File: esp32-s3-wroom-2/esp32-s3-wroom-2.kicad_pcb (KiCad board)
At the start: 4 copper layers, 11 parts, among them SW1 SW_Push, SW2 SW_Push, U1 ESP32-S3-WROOM-2

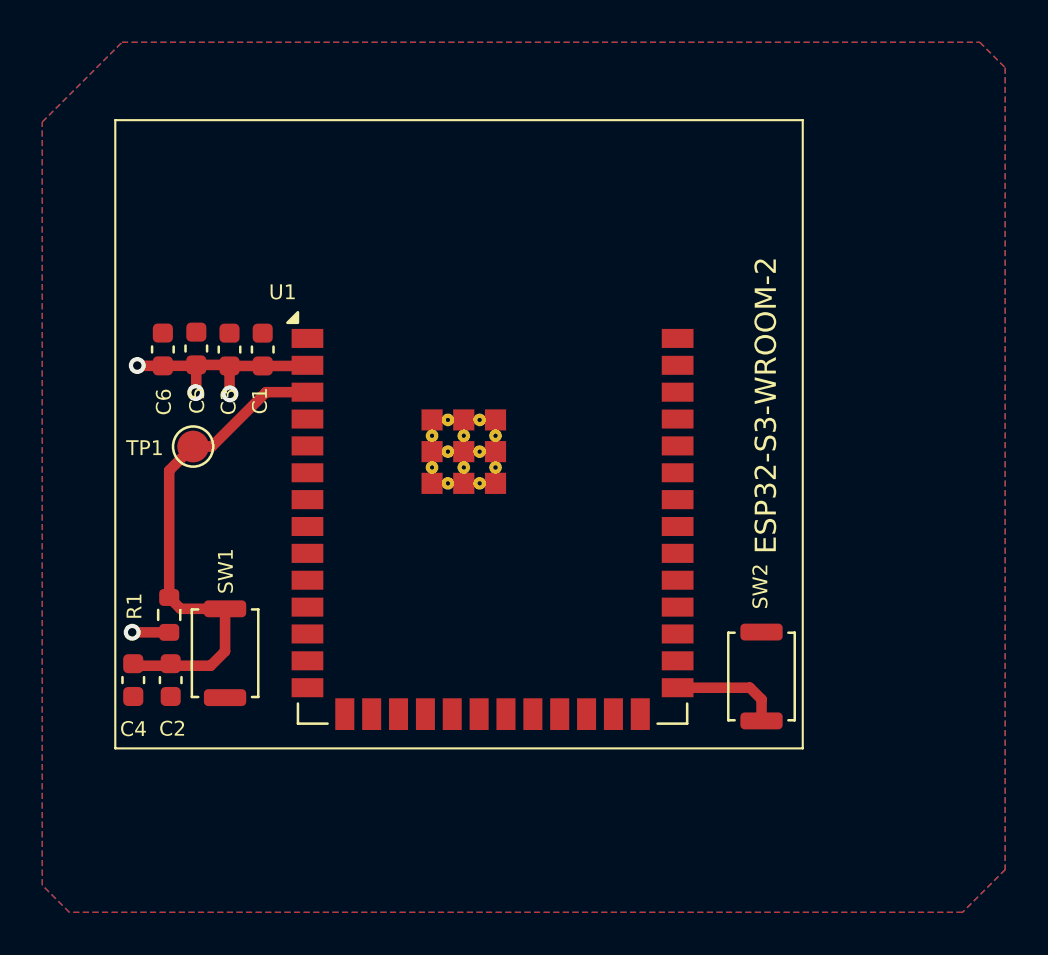
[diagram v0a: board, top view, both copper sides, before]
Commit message: [Rushil] corrected pcb added information on both schematic and pcb user drawing correct circuit of bno055
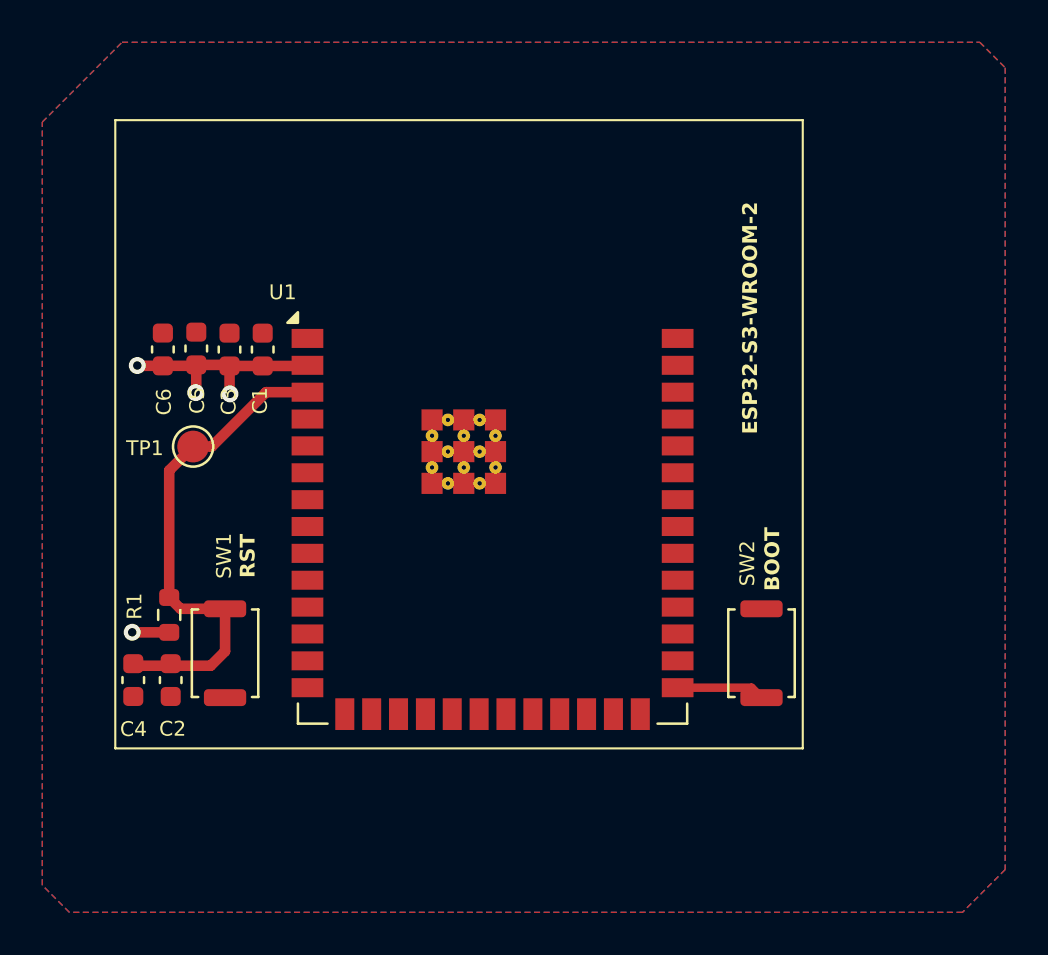
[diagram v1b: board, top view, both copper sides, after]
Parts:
- SW1: value SW_Push -> RST
- SW2: value SW_Push -> BOOT
- TP1: value TestPoint -> T_EN
- moved SW2 1.10 mm to (90.4, 74.1)
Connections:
- net /block_ESP32-S3-WROOM-2/+3V3 renamed /block_esp32-s3-wroom-2/+3V3
- net /block_ESP32-S3-WROOM-2/GND renamed /block_esp32-s3-wroom-2/GND
- net /block_ESP32-S3-WROOM-2/IO1 renamed /block_esp32-s3-wroom-2/IO1
- net /block_ESP32-S3-WROOM-2/IO10 renamed /block_esp32-s3-wroom-2/IO10
- net /block_ESP32-S3-WROOM-2/IO11 renamed /block_esp32-s3-wroom-2/IO11
- net /block_ESP32-S3-WROOM-2/IO12 renamed /block_esp32-s3-wroom-2/IO12
- net /block_ESP32-S3-WROOM-2/IO13 renamed /block_esp32-s3-wroom-2/IO13
- net /block_ESP32-S3-WROOM-2/IO14 renamed /block_esp32-s3-wroom-2/IO14
- net /block_ESP32-S3-WROOM-2/IO15 renamed /block_esp32-s3-wroom-2/IO15
- net /block_ESP32-S3-WROOM-2/IO16 renamed /block_esp32-s3-wroom-2/IO16
- net /block_ESP32-S3-WROOM-2/IO17 renamed /block_esp32-s3-wroom-2/IO17
- net /block_ESP32-S3-WROOM-2/IO18 renamed /block_esp32-s3-wroom-2/IO18
- net /block_ESP32-S3-WROOM-2/IO2 renamed /block_esp32-s3-wroom-2/IO2
- net /block_ESP32-S3-WROOM-2/IO21 renamed /block_esp32-s3-wroom-2/IO21
- net /block_ESP32-S3-WROOM-2/IO3 renamed /block_esp32-s3-wroom-2/IO3
- net /block_ESP32-S3-WROOM-2/IO38 renamed /block_esp32-s3-wroom-2/IO38
- net /block_ESP32-S3-WROOM-2/IO4 renamed /block_esp32-s3-wroom-2/IO4
- net /block_ESP32-S3-WROOM-2/IO45 renamed /block_esp32-s3-wroom-2/IO45
- net /block_ESP32-S3-WROOM-2/IO46 renamed /block_esp32-s3-wroom-2/IO46
- net /block_ESP32-S3-WROOM-2/IO47 renamed /block_esp32-s3-wroom-2/IO47
- net /block_ESP32-S3-WROOM-2/IO48 renamed /block_esp32-s3-wroom-2/IO48
- net /block_ESP32-S3-WROOM-2/IO5 renamed /block_esp32-s3-wroom-2/IO5
- net /block_ESP32-S3-WROOM-2/IO6 renamed /block_esp32-s3-wroom-2/IO6
- net /block_ESP32-S3-WROOM-2/IO7 renamed /block_esp32-s3-wroom-2/IO7
- net /block_ESP32-S3-WROOM-2/IO8 renamed /block_esp32-s3-wroom-2/IO8
- net /block_ESP32-S3-WROOM-2/IO9 renamed /block_esp32-s3-wroom-2/IO9
- net /block_ESP32-S3-WROOM-2/MTCK/IO39 renamed /block_esp32-s3-wroom-2/MTCK/IO39
- net /block_ESP32-S3-WROOM-2/MTDI/IO41 renamed /block_esp32-s3-wroom-2/MTDI/IO41
- net /block_ESP32-S3-WROOM-2/MTDO/IO40 renamed /block_esp32-s3-wroom-2/MTDO/IO40
- net /block_ESP32-S3-WROOM-2/MTMS/IO42 renamed /block_esp32-s3-wroom-2/MTMS/IO42
- net /block_ESP32-S3-WROOM-2/RXD0/IO44 renamed /block_esp32-s3-wroom-2/RXD0/IO44
- net /block_ESP32-S3-WROOM-2/TXD0/IO43 renamed /block_esp32-s3-wroom-2/TXD0/IO43
- net /block_ESP32-S3-WROOM-2/USB_D+ renamed /block_esp32-s3-wroom-2/USB_D+
- net /block_ESP32-S3-WROOM-2/USB_D- renamed /block_esp32-s3-wroom-2/USB_D-
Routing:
- net Net-(U1-IO0): track 5.21 -> 4.16 mm
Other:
- board text added: "ANTENNA"
- board text added: "Don't use high noise switching elements near antenna"
- board text added: "ESP32-S3-WROOM-2 2.4 GHz WiFi + BLE 5 RISC-V Dual-Core MCU 3.3 V Operation"
- board text added: "• Keep decoupling capacitors close to VDD pins. • Avoid placing high-speed or high-current traces under module. • Keep antenna region clear of copper pour, switching regulators, and ground planes. • Maintain solid GND plane under module (except antenna zone)."
- board text removed: "Avoid placing it near high switching circuits or high current trace"

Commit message: [Rushil] fixed block esp32 wroom
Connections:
- net /block_esp32-s3-wroom-2/+3V3 renamed /esp32-s3-wroom-2/3V3
- net /block_esp32-s3-wroom-2/GND renamed /esp32-s3-wroom-2/GND
- net /block_esp32-s3-wroom-2/IO1 renamed /esp32-s3-wroom-2/IO1
- net /block_esp32-s3-wroom-2/IO10 renamed /esp32-s3-wroom-2/IO10
- net /block_esp32-s3-wroom-2/IO11 renamed /esp32-s3-wroom-2/IO11
- net /block_esp32-s3-wroom-2/IO12 renamed /esp32-s3-wroom-2/IO12
- net /block_esp32-s3-wroom-2/IO13 renamed /esp32-s3-wroom-2/IO13
- net /block_esp32-s3-wroom-2/IO14 renamed /esp32-s3-wroom-2/IO14
- net /block_esp32-s3-wroom-2/IO15 renamed /esp32-s3-wroom-2/IO15
- net /block_esp32-s3-wroom-2/IO16 renamed /esp32-s3-wroom-2/IO16
- net /block_esp32-s3-wroom-2/IO17 renamed /esp32-s3-wroom-2/IO17
- net /block_esp32-s3-wroom-2/IO18 renamed /esp32-s3-wroom-2/IO18
- net /block_esp32-s3-wroom-2/IO2 renamed /esp32-s3-wroom-2/IO2
- net /block_esp32-s3-wroom-2/IO21 renamed /esp32-s3-wroom-2/IO21
- net /block_esp32-s3-wroom-2/IO3 renamed /esp32-s3-wroom-2/IO3
- net /block_esp32-s3-wroom-2/IO38 renamed /esp32-s3-wroom-2/IO38
- net /block_esp32-s3-wroom-2/IO4 renamed /esp32-s3-wroom-2/IO4
- net /block_esp32-s3-wroom-2/IO45 renamed /esp32-s3-wroom-2/IO45
- net /block_esp32-s3-wroom-2/IO46 renamed /esp32-s3-wroom-2/IO46
- net /block_esp32-s3-wroom-2/IO47 renamed /esp32-s3-wroom-2/IO47
- net /block_esp32-s3-wroom-2/IO48 renamed /esp32-s3-wroom-2/IO48
- net /block_esp32-s3-wroom-2/IO5 renamed /esp32-s3-wroom-2/IO5
- net /block_esp32-s3-wroom-2/IO6 renamed /esp32-s3-wroom-2/IO6
- net /block_esp32-s3-wroom-2/IO7 renamed /esp32-s3-wroom-2/IO7
- net /block_esp32-s3-wroom-2/IO8 renamed /esp32-s3-wroom-2/IO8
- net /block_esp32-s3-wroom-2/IO9 renamed /esp32-s3-wroom-2/IO9
- net /block_esp32-s3-wroom-2/MTCK/IO39 renamed /esp32-s3-wroom-2/MTCK/IO39
- net /block_esp32-s3-wroom-2/MTDI/IO41 renamed /esp32-s3-wroom-2/MTDI/IO41
- net /block_esp32-s3-wroom-2/MTDO/IO40 renamed /esp32-s3-wroom-2/MTDO/IO40
- net /block_esp32-s3-wroom-2/MTMS/IO42 renamed /esp32-s3-wroom-2/MTMS/IO42
- net /block_esp32-s3-wroom-2/RXD0/IO44 renamed /esp32-s3-wroom-2/RXD0/IO44
- net /block_esp32-s3-wroom-2/TXD0/IO43 renamed /esp32-s3-wroom-2/TXD0/IO43
- net /block_esp32-s3-wroom-2/USB_D+ renamed /esp32-s3-wroom-2/USB_D+
- net /block_esp32-s3-wroom-2/USB_D- renamed /esp32-s3-wroom-2/USB_D-
